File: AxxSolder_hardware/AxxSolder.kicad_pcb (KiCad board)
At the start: 2 copper layers, 39 x 82.5 mm, 126 parts, among them IC1 OPA2387DSGT, IC3 TPS54302DDCR, IC4 STUSB4500QTR, IC5 LTC4440AHMS8E, IC6 MAX16171ATA_VY+T, IC7 STM32G431CBT6, J1 USB4110-GF-A, J2 691243110009, J3 Conn_01x05_Socket, Q1 STL9P3LLH6, Q2 2N7002NXAKR, Q3 STL10N3LLH5, U3 PEC11J-9220F-S0015, U4 BSC014N04LS

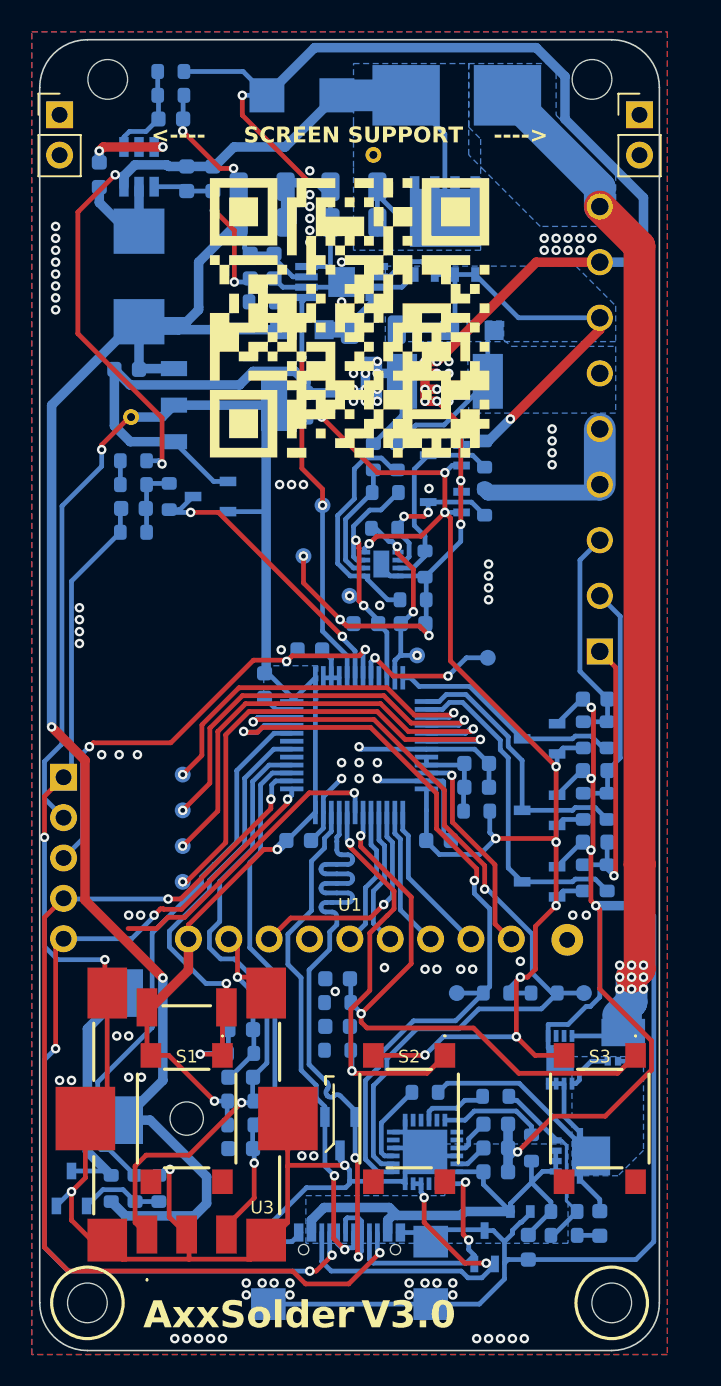
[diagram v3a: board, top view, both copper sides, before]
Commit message: Update grounding layout and adding a fuse
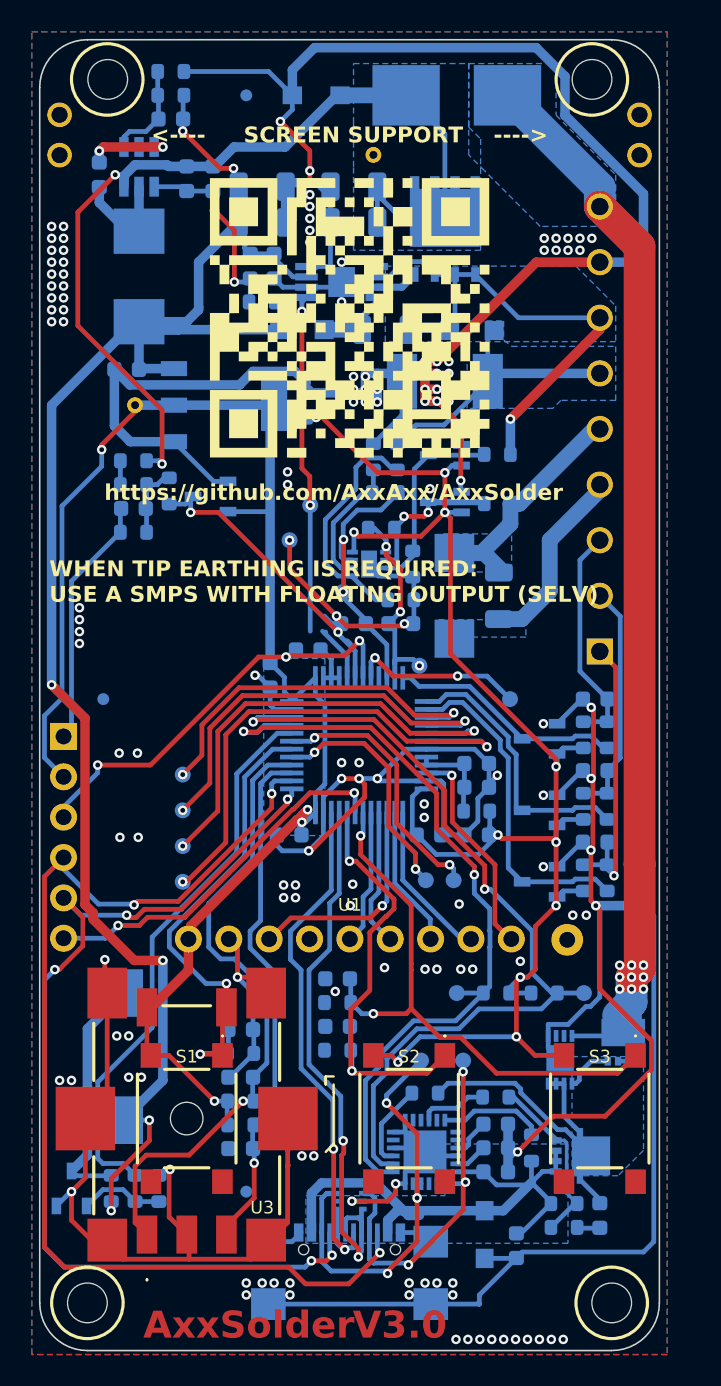
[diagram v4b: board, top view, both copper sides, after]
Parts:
- removed C17, C18: 10u, Capacitor_SMD:C_0603_1608Metric
- removed D11: ESDA25P35, footprints:ESDA25P351U1M
- removed D12: TPD2E2U06, footprints:SOT95P237X95-3N
- added C12: 10u, Capacitor_SMD:C_0603_1608Metric, B.Cu at (189.7, 135.8)
- added C15: 10u, Capacitor_SMD:C_0603_1608Metric, B.Cu at (189.7, 137.2)
- added C3: 10u, Capacitor_SMD:C_0603_1608Metric, B.Cu at (188.5, 117.5)
- added F2: SF-2410FP100W-2, footprints:SF2410FP100W2, B.Cu at (187.1, 102.5)
- added FID1: Fiducial, Fiducial:Fiducial_0.75mm_Mask1.5mm, B.Cu at (174.0, 71.0)
- added FID2: Fiducial, Fiducial:Fiducial_0.75mm_Mask1.5mm, B.Cu at (174.0, 140.0)
- added FID3: Fiducial, Fiducial:Fiducial_0.75mm_Mask1.5mm, B.Cu at (165.0, 109.0)
- added IC2: TPD4E1B06DRLR, footprints:SOTFL50P160X60-6N, B.Cu at (180.5, 140.6)
- added R40: 1M, Resistor_SMD:R_1206_3216Metric, B.Cu at (189.9, 102.5)
- added TP16: DIAG_TP, TestPoint:TestPoint_Pad_D1.0mm, B.Cu at (187.7, 131.8)
- added TP17: DIAG_TP, TestPoint:TestPoint_Pad_D1.0mm, B.Cu at (185.0, 131.8)
- added TP18: DIAG_TP, TestPoint:TestPoint_Pad_D1.0mm, B.Cu at (187.1, 120.4)
- added TP19: DIAG_TP, TestPoint:TestPoint_Pad_D1.0mm, B.Cu at (185.3, 120.4)
- D3: value ESDA25W -> SMF4L24AT1G; footprint footprints:SOT65P210X110-3N -> footprints:SODFL3619X98N
- D4: value SMBJ24A -> SMF4L24AT1G; footprint footprints:DIOM5436X261N -> footprints:SODFL3619X98N
- J2: value 691243110009 -> 691243110008
- J3: value Conn_01x05_Socket -> 61300611821; footprint Connector_PinSocket_2.54mm:PinSocket_1x05_P2.54mm_Vertical -> footprints:RHDR6W97P0X254_1X6_1574X250X865P
- REF** (x2): value PinHeader_1x02_P2.54mm_Vertical -> TSW-102-XX-YY-S; footprint Connector_PinHeader_2.54mm:PinHeader_1x02_P2.54mm_Vertical -> footprints:TSW-102-XX-YY-S; moved to B.Cu
- moved TP15 2.95 mm to (190.6, 109.0)
- moved J3 2.57 mm to (162.5, 111.3), turned to -90 degrees
- moved TP14 1.33 mm to (176.7, 99.0)
- moved D4 0.90 mm to (178.4, 71.0)
- moved R5 0.81 mm to (189.8, 96.7), turned to 180 degrees
- moved R1 0.80 mm to (189.8, 93.6), turned to 180 degrees
- moved D3 0.80 mm to (189.0, 142.7), turned to -90 degrees
- moved TP2 0.79 mm to (167.0, 90.5)
- moved C10 0.78 mm to (183.7, 104.2)
- moved C11 0.78 mm to (180.8, 104.2)
- moved IC1 0.78 mm to (181.7, 100.5)
- moved R2 0.78 mm to (184.5, 100.5)
- moved R3 0.78 mm to (183.7, 102.8)
- moved TP8 0.78 mm to (178.0, 96.8)
- moved C19 0.76 mm to (191.0, 143.4)
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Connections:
- net /Handle_sense1 renamed /H_sense1
- net /Handle_sense2 renamed /H_sense2
- net /Stand_sense renamed /S_sense
- D3 pad 1: /CC2 -> /VBUS
- D3 pad 2: /CC1 -> GND
- IC7 pad 41: unconnected-(IC7-PB4-Pad41) -> /CC2_
- IC7 pad 43: unconnected-(IC7-PB6-Pad43) -> /CC1_
- J2 pad 4: /GREEN -> Earth
- R10 pad 1: Net-(IC3-FB) -> GND
- R10 pad 2: GND -> Net-(IC3-FB)
- R13 pad 1: /VBUS -> Net-(IC4-VBUS_VS_DISCH)
- R13 pad 2: Net-(IC4-VBUS_VS_DISCH) -> /VBUS
- R15 pad 1: /VDD_IN_USBCPD -> Net-(IC4-DISCH)
- R15 pad 2: Net-(IC4-DISCH) -> /VDD_IN_USBCPD
- R21 pad 1: Net-(R21-Pad1) -> Net-(C29-Pad1)
- R21 pad 2: Net-(C29-Pad1) -> Net-(R21-Pad2)
- R41 pad 1: VDD -> Net-(R21-Pad2)
- R41 pad 2: Net-(R21-Pad1) -> VDD
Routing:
- net GND: track 504.8 -> 478.2 mm, vias 137 -> 146
- net /CC1_: track 0.00 -> 16.7 mm, vias 0 -> 2
- net /CC2_: track 0.00 -> 15.1 mm, vias 0 -> 2
- net Earth: track 0.00 -> 11.8 mm
- net /CC1: track 15.4 -> 25.3 mm, vias 2 -> 3
- net /USB_D-: track 45.0 -> 35.9 mm
- net /BLUE: track 10.7 -> 17.9 mm
- net +3.3V: track 197.4 -> 204.1 mm, vias 14 -> 15
- net +6V: track 117.5 -> 112.3 mm, vias 4 -> 6
- net /USART_TX: track 19.0 -> 24.1 mm, vias 1 -> 2
- net /CC2: track 22.1 -> 27.0 mm, vias 2 -> 3
- net /SWCLK: track 65.0 -> 69.4 mm
- net /VBUS: track 31.6 -> 35.6 mm
- net /SWDIO: track 59.3 -> 62.7 mm
- net /NRST: track 30.5 -> 27.4 mm
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- added copper zone on B.Cu, net /GREEN
- added copper zone on B.Cu, net Earth
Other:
- board text added: "2024-01"
- board text added: "DON'T SOLDER ON LIVE CIRCUITS!"
- board text added: "G431CBT6"
- board text added: "PWM"
- board text added: "STM32"
- board text added: "TX"
- board text added: "WHEN TIP EARTHING IS REQUIRED: USE A SMPS WITH FLOATING OUTPUT (SELV)"
- board text added: "https://github.com/AxxAxx/AxxSolder"
- board text removed: "2025-01"
- board text removed: "SW"

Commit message: Updates on PCB before ordering
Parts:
- removed TP15: DIAG_TP, TestPoint:TestPoint_Pad_D1.0mm
- added J4: TSW-102-07-T-S, footprints:TSW-102-XX-YY-S, F.Cu at (2.50, 2.50)
- added J5: TSW-102-07-T-S, footprints:TSW-102-XX-YY-S, F.Cu at (2.50, 8.87)
- J2: value 691243110008 -> 691243110009
- moved C2 11.2 mm to (166.5, 90.5), turned to 180 degrees
- moved FID3 3.16 mm to (168.0, 110.0)
- moved TP2 1.80 mm to (167.0, 92.3)
- moved C34 0.91 mm to (173.7, 138.2)
- moved R33 0.91 mm to (173.7, 136.7)
- moved IC5 0.72 mm to (179.7, 82.1)
- moved TP17 0.70 mm to (185.7, 131.8)
- moved TP4 0.40 mm to (179.7, 102.2)
- moved TP18 0.32 mm to (187.4, 120.4)
- moved R8 0.25 mm to (182.5, 98.0)
- moved LS1 0.15 mm to (166.1, 131.2)
- moved TP19 0.13 mm to (185.4, 120.4)
- moved C26 0.10 mm to (173.7, 129.7)
- moved C33 0.10 mm to (173.7, 132.7)
- moved R27 0.10 mm to (173.7, 131.2)
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- renumbered REF** to J4, REF** to J5
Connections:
- IC7 pad 15: /USR1 -> unconnected-(IC7-PA7-Pad15)
- IC7 pad 30: /SW3 -> unconnected-(IC7-PA8-Pad30)
- IC7 pad 39: /ENC_A -> /SCL
- IC7 pad 45: /SCL -> /SW3
- IC7 pad 8: /GROUND_DET -> /ENC_A
- IC7 pad 9: unconnected-(IC7-PA1-Pad9) -> /USR1
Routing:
- net /SW3: track 35.7 -> 47.1 mm
- net /GROUND_DET: track 10.9 -> 0.00 mm, vias 2 -> 0
- net /ENC_A: track 32.9 -> 41.0 mm, vias 1 -> 3
- net /SCL: track 50.2 -> 43.6 mm
- net /USR1: track 23.1 -> 17.2 mm
- net +3.3V: track 204.1 -> 200.4 mm
- net GND: track 478.2 -> 481.5 mm, vias 146 -> 132
- net /VDD_IN_USBCPD: track 19.6 -> 22.7 mm
- net /SDA: track 54.6 -> 52.6 mm
- net +6V: track 112.3 -> 110.7 mm
- net /CC2_: track 15.1 -> 16.5 mm
- net /Heater: track 27.1 -> 28.4 mm
- net /CC1: track 25.3 -> 24.2 mm
- net /SWDIO: track 62.7 -> 61.7 mm
- net /CC2: track 27.0 -> 27.8 mm
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- removed copper zone on B.Cu, net +3.3V
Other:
- board text added: "9-24 VDC"
- board text added: "AxxAxx"
- board text added: "BOOT0"
- board text added: "NEVER SOLDER ON LIVE CIRCUITS!"
- board text added: "SWD"
- board text added: "WHEN TIP EARTHING IS REQUIRED: USE A SUPPLY WITH FLOATING OUTPUT (SELV)"
- board text added: "WayWayWay"
- board text removed: "9-24 V"
- board text removed: "DON'T SOLDER ON LIVE CIRCUITS!"
- board text removed: "WHEN TIP EARTHING IS REQUIRED: USE A SMPS WITH FLOATING OUTPUT (SELV)"

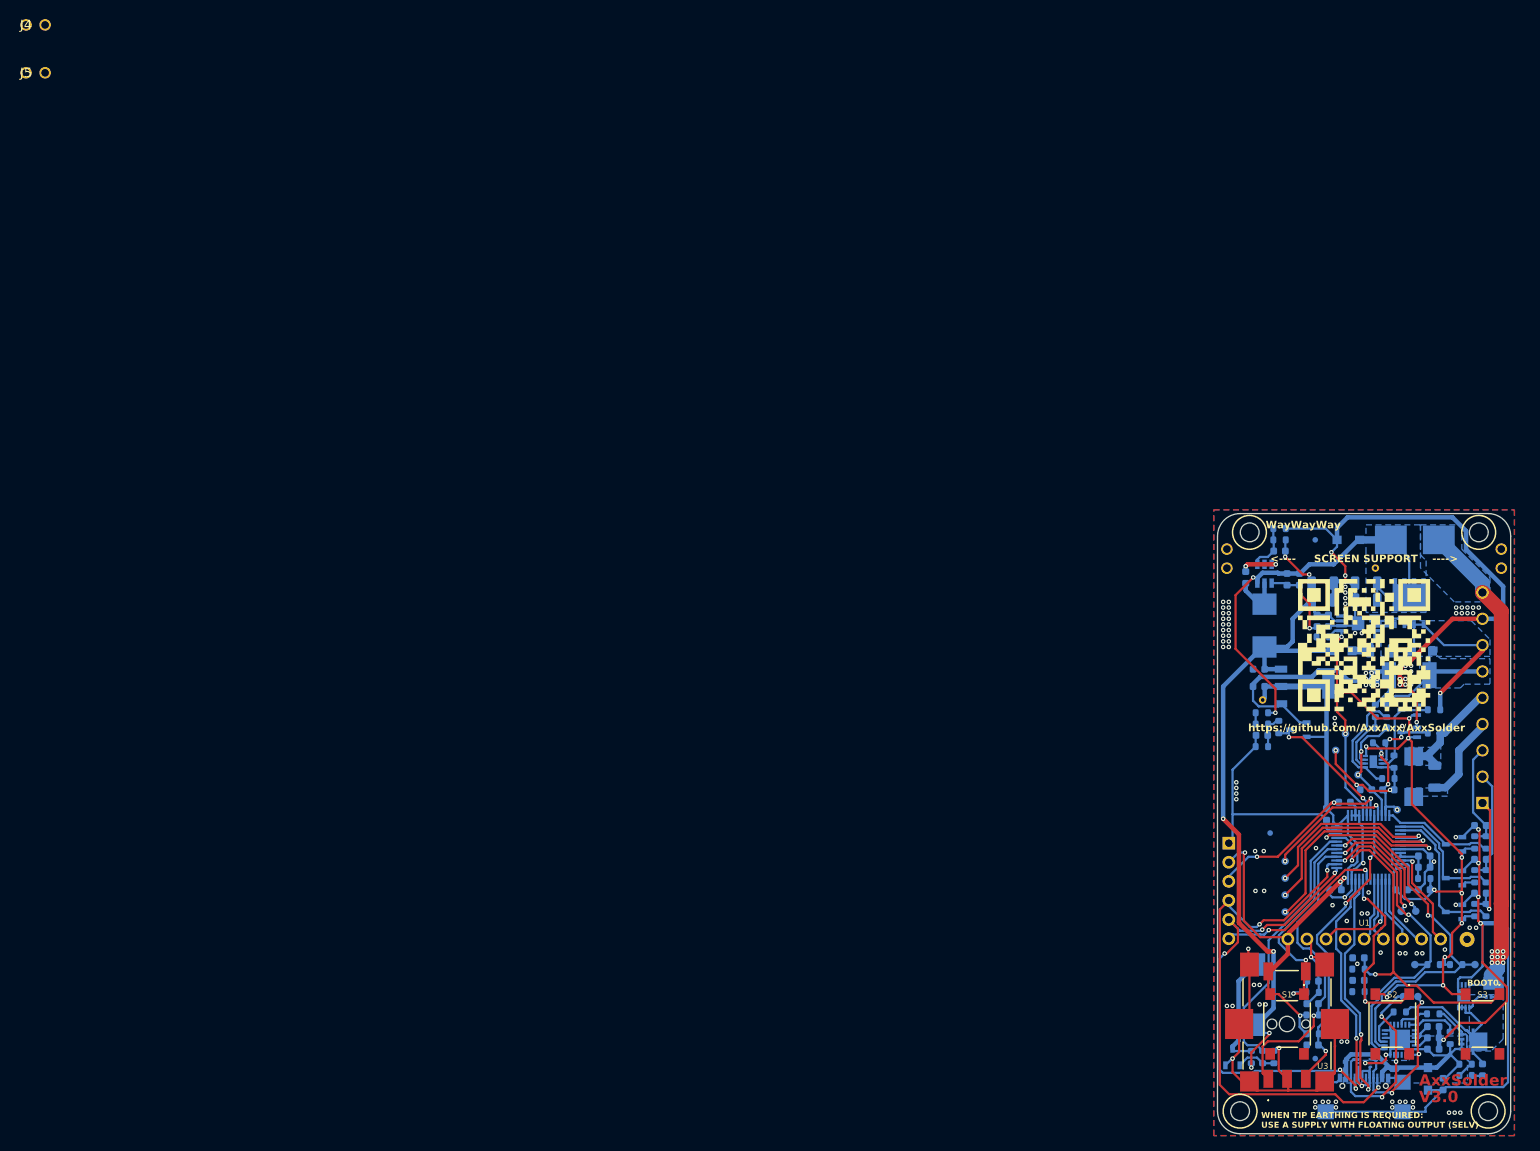
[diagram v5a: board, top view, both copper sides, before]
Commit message: update BOM and PCB dawing
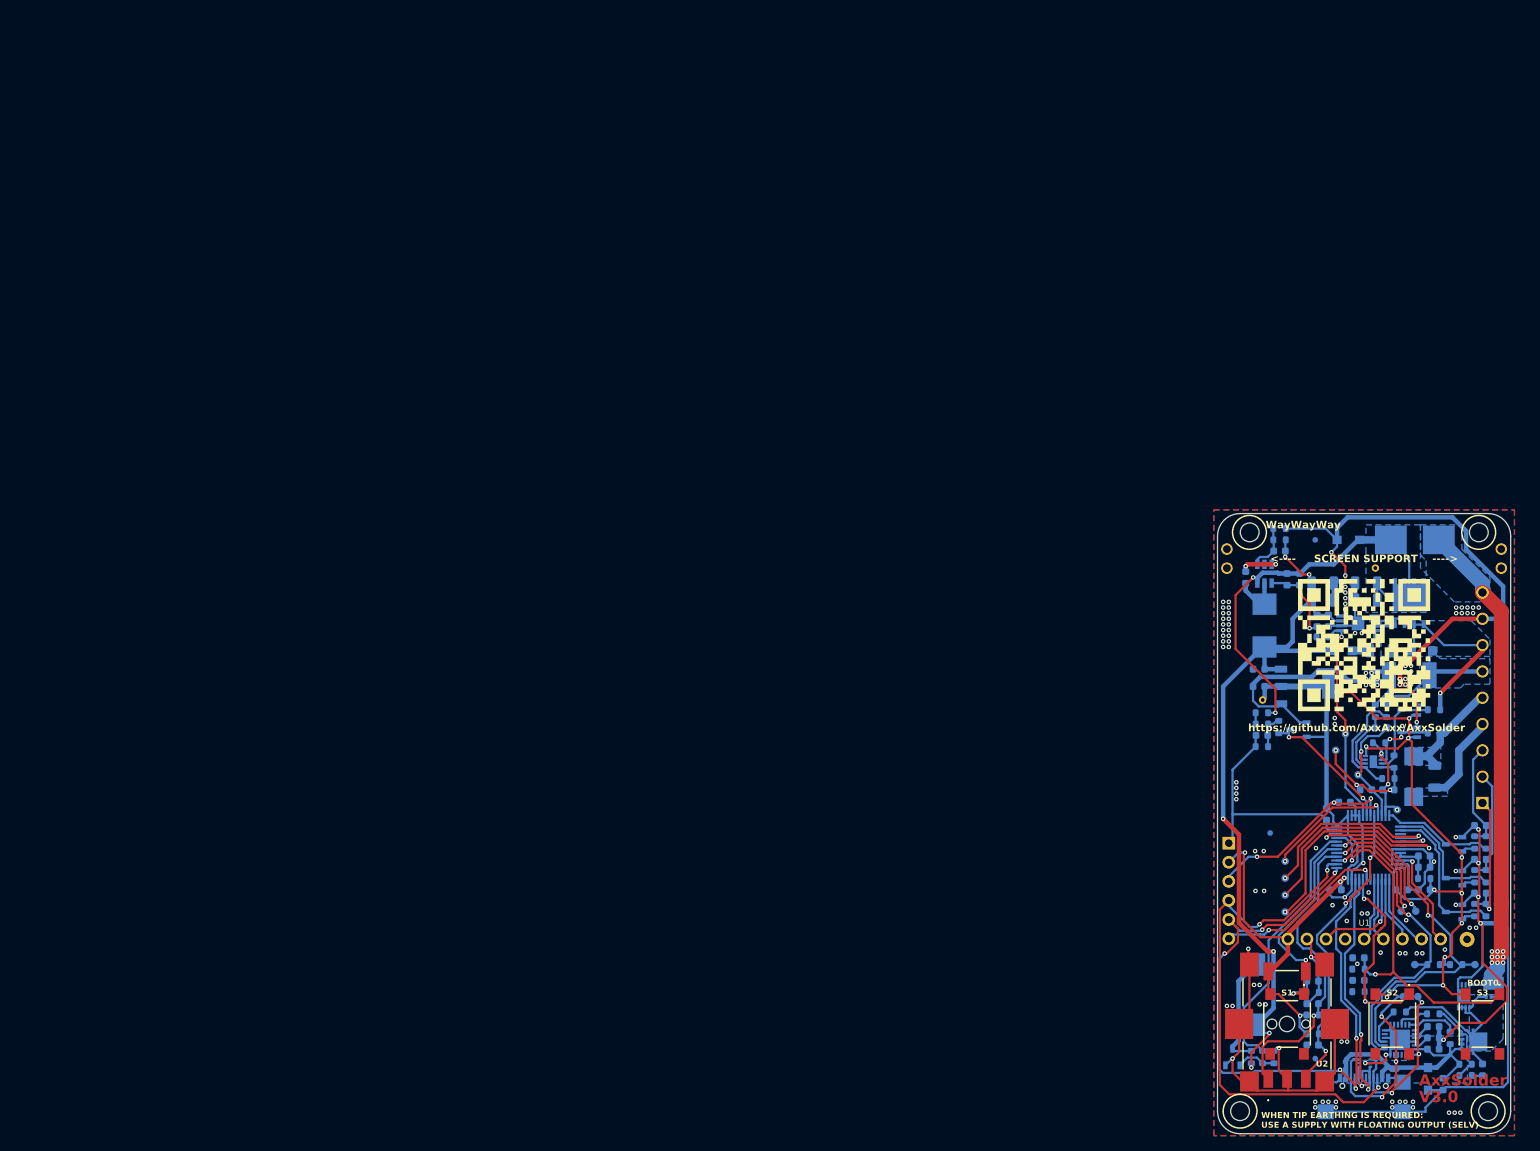
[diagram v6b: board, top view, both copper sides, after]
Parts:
- removed the J4 at (162.2, 72.2)
- removed the J5 at (198.8, 72.2)
- removed U3: PEC11J-9220F-S0015, footprints:PEC11J9220FS0015
- added U2: PEC11J-9215F-S0015, footprints:PEC11J9215FS0015, F.Cu at (170.2, 135.4)
- S1, S2, S3: value ADTSM644KVTR -> ADTSM644RVTR; footprint footprints:ADTSM644KVTR -> footprints:ADTSM644RVTR
- moved J5 206.2 mm to (198.8, 72.2), turned to -90 degrees
- moved J4 174.3 mm to (162.2, 72.2), turned to -90 degrees
